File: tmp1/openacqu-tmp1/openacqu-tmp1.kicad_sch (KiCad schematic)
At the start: 0 parts

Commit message: Added sensor to tmp1
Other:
- added sheet Temp_sensor (temp_sensor.kicad_sch)
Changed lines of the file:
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@@
 		)
 		(instances
-			(project "openacqu-core"
+			(project "openacqu-tmp1"
 				(path "/2621f8e5-8f03-4409-8fc3-1378e1ab4580"
 					(page "2")
 				)
 			)
+		)
+	)
+	(sheet
+		(at 88.9 49.53)
+		(size 25.4 10.16)
+		(exclude_from_sim no)
+		(in_bom yes)
+		(on_board yes)
+		(dnp no)
+		(fields_autoplaced yes)
+		(stroke
+			(width 0.1524)
+			(type solid)
+		)
+		(fill
+			(color 0 0 0 0.0000)
+		)
+		(property "Sheetname" "Temp_sensor"
+			(at 88.9 48.8184 0)
+			(effects
+				(font
+					(size 1.27 1.27)
+				)
+				(justify left bottom)
+			)
+		)
+		(property "Sheetfile" "temp_sensor.kicad_sch"
+			(at 88.9 60.2746 0)
+			(effects
+				(font
+					(size 1.27 1.27)
+				)
+				(justify left top)
+			)
+		)
+		(instances
+			(project "openacqu-tmp1"
+				(path "/2621f8e5-8f03-4409-8fc3-1378e1ab4580"
+					(page "3")
+				)
+			)

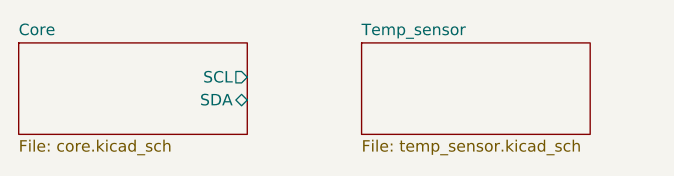
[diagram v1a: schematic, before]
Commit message: Completed layout for the TMP1
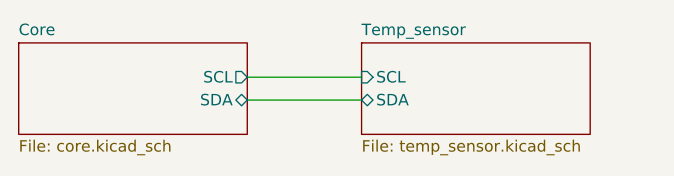
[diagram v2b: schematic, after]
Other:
- sheet Temp_sensor ports: added SCL, SDA; removed none
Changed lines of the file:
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@@
 	(generator_version "9.0")
 	(paper "A4")
+	(wire
+		(pts
+			(xy 76.2 53.34) (xy 88.9 53.34)
+		)
+		(stroke
+			(width 0)
+			(type default)
+		)
+	)
+	(wire
+		(pts
+			(xy 76.2 55.88) (xy 88.9 55.88)
+		)
+		(stroke
+			(width 0)
+			(type default)
+		)
+	)
 	(sheet
 		(at 50.8 49.53)
@@
 			)
 		)
+		(pin "SCL" input
+			(at 88.9 53.34 180)
+			(effects
+				(font
+					(size 1.27 1.27)
+				)
+				(justify left)
+			)
+		)
+		(pin "SDA" bidirectional
+			(at 88.9 55.88 180)
+			(effects
+				(font
+					(size 1.27 1.27)
+				)
+				(justify left)
+			)
+		)
